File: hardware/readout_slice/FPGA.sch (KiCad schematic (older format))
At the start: 33 parts

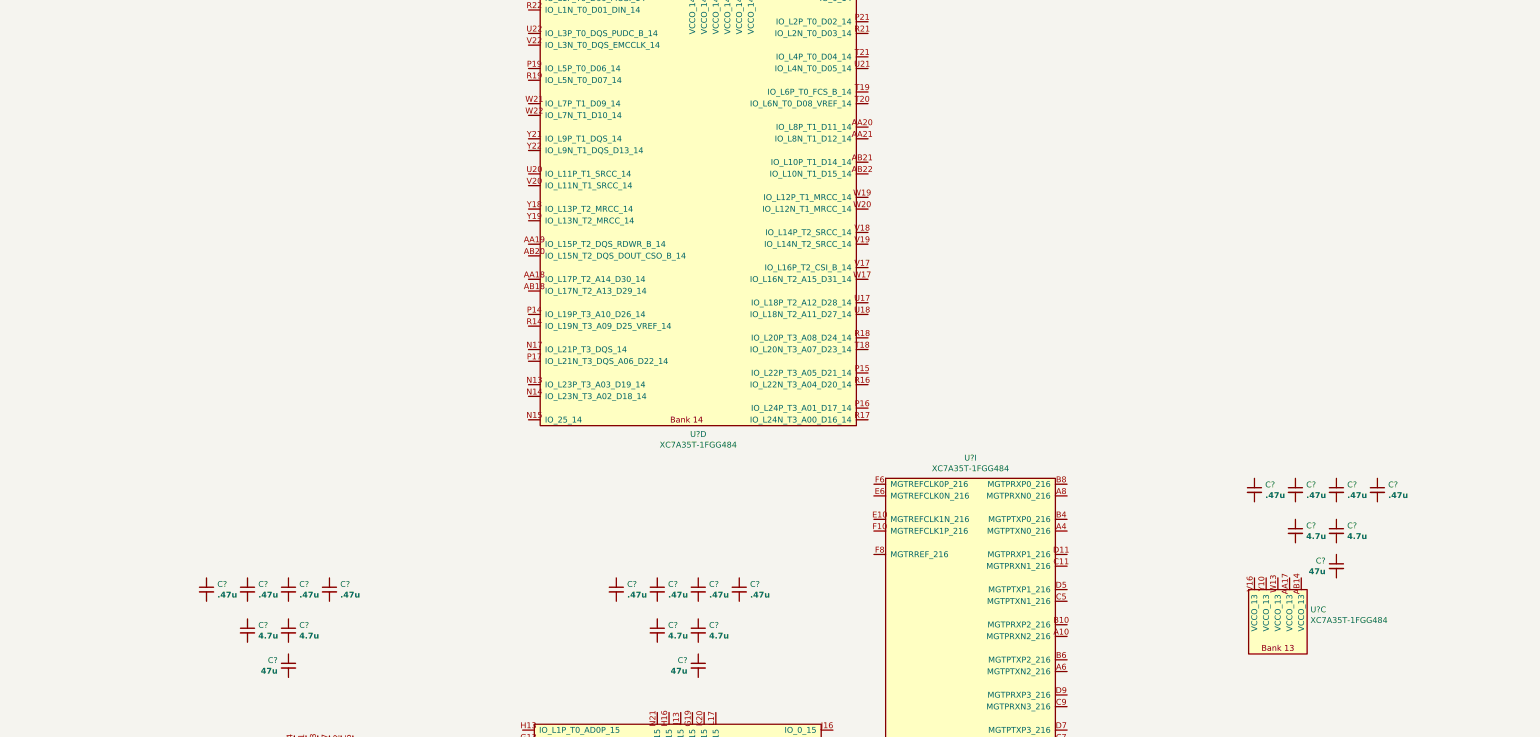
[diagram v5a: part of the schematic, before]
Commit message: readout_slice is more ordered now
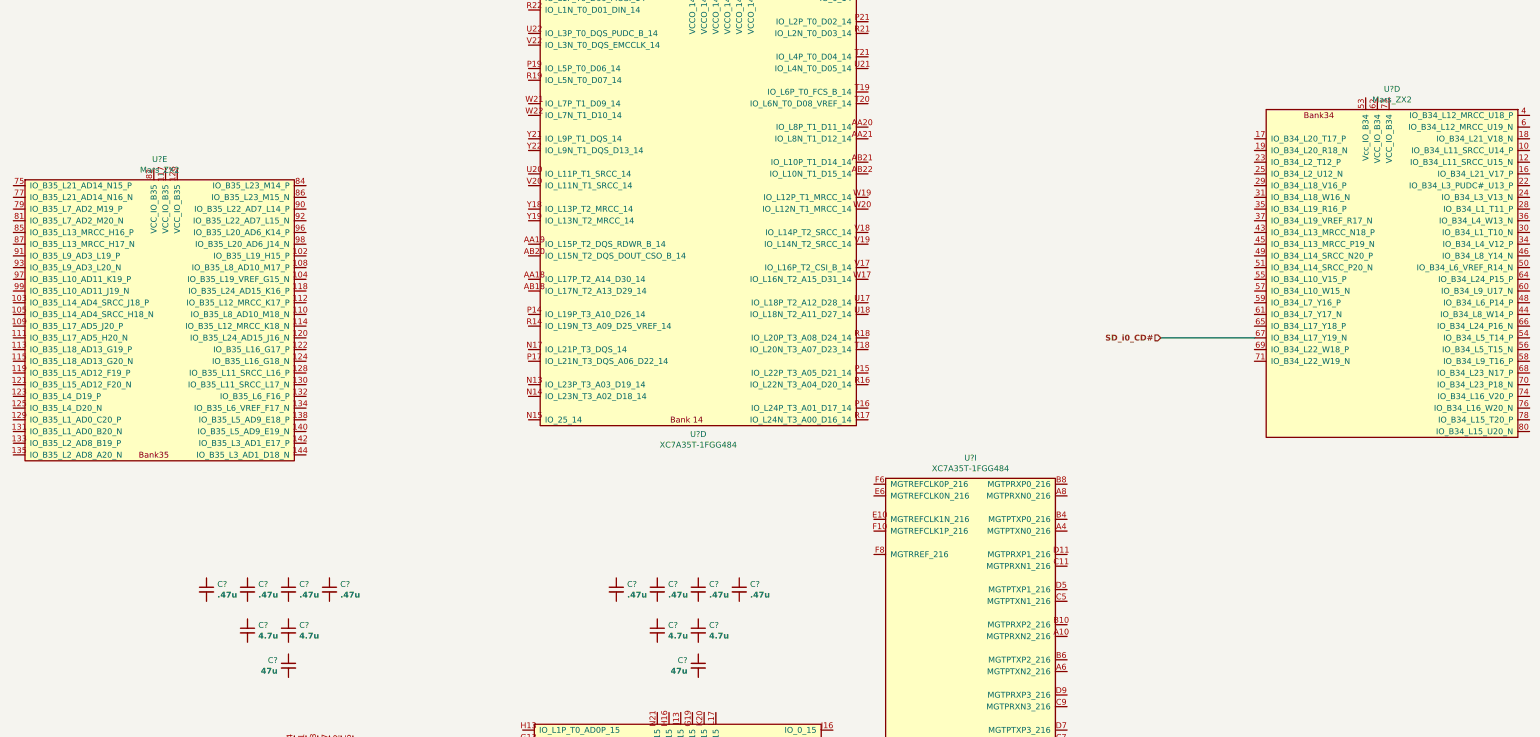
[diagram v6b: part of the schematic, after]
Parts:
- removed C?: 47u, symbol Device:C_Small
- removed C? (x2): 4.7u, symbol Device:C_Small
- removed C? (x4): .47u, symbol Device:C_Small
- removed U?: XC7A35T-1FGG484, symbol readout:XC7A35T-1FGG484
- added U? (x2): Mars_ZX2, Package_QFP:LQFP-160_24x24mm_P0.5mm, symbol readout:Mars_ZX2
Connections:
- new net SD_i0_CD#: U?.67 (IO_B34_L17_Y19_N)
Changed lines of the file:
@@
 $Descr A4 11693 8268
 encoding utf-8
-Sheet 3 6
+Sheet 2 10
 Title ""
 Date ""
@@
 $Comp
 L readout:XC7A35T-1FGG484 U?
-U 3 1 604BC08F
-P 10000 4800
-F 0 "U?" H 10278 4629 50  0000 L CNN
-F 1 "XC7A35T-1FGG484" H 10278 4538 50  0000 L CNN
-F 2 "" H 8900 4950 50  0001 C CNN
-F 3 "" H 8900 4950 50  0001 C CNN
-	3    10000 4800
-	1    0    0    -1
-$EndComp
-$Comp
-L readout:XC7A35T-1FGG484 U?
 U 4 1 604C5353
 P 5000 -300
@@
 	5500 -900 5500 -450
 Connection ~ 5500 -450
-$Comp
-L Device:C_Small C?
-U 1 1 6050AA4C
-P 10500 4600
-F 0 "C?" H 10408 4646 50  0000 R CNN
-F 1 "47u" H 10408 4555 50  0000 R CNB
-F 2 "" H 10500 4600 50  0001 C CNN
-F 3 "~" H 10500 4600 50  0001 C CNN
-	1    10500 4600
-	1    0    0    -1
-$EndComp
-$Comp
-L Device:C_Small C?
-U 1 1 6050AA52
-P 10500 4300
-F 0 "C?" H 10592 4346 50  0000 L CNN
-F 1 "4.7u" H 10592 4255 50  0000 L CNB
-F 2 "" H 10500 4300 50  0001 C CNN
-F 3 "~" H 10500 4300 50  0001 C CNN
-	1    10500 4300
-	1    0    0    -1
-$EndComp
-$Comp
-L Device:C_Small C?
-U 1 1 6050AA58
-P 10150 4300
-F 0 "C?" H 10242 4346 50  0000 L CNN
-F 1 "4.7u" H 10242 4255 50  0000 L CNB
-F 2 "" H 10150 4300 50  0001 C CNN
-F 3 "~" H 10150 4300 50  0001 C CNN
-	1    10150 4300
-	1    0    0    -1
-$EndComp
-$Comp
-L Device:C_Small C?
-U 1 1 6050AA5E
-P 9800 3950
-F 0 "C?" H 9892 3996 50  0000 L CNN
-F 1 ".47u" H 9892 3905 50  0000 L CNB
-F 2 "" H 9800 3950 50  0001 C CNN
-F 3 "~" H 9800 3950 50  0001 C CNN
-	1    9800 3950
-	1    0    0    -1
-$EndComp
-$Comp
-L Device:C_Small C?
-U 1 1 6050AA64
-P 10150 3950
-F 0 "C?" H 10242 3996 50  0000 L CNN
-F 1 ".47u" H 10242 3905 50  0000 L CNB
-F 2 "" H 10150 3950 50  0001 C CNN
-F 3 "~" H 10150 3950 50  0001 C CNN
-	1    10150 3950
-	1    0    0    -1
-$EndComp
-$Comp
-L Device:C_Small C?
-U 1 1 6050AA6A
-P 10500 3950
-F 0 "C?" H 10592 3996 50  0000 L CNN
-F 1 ".47u" H 10592 3905 50  0000 L CNB
-F 2 "" H 10500 3950 50  0001 C CNN
-F 3 "~" H 10500 3950 50  0001 C CNN
-	1    10500 3950
-	1    0    0    -1
-$EndComp
-$Comp
-L Device:C_Small C?
-U 1 1 6050AA70
-P 10850 3950
-F 0 "C?" H 10942 3996 50  0000 L CNN
-F 1 ".47u" H 10942 3905 50  0000 L CNB
-F 2 "" H 10850 3950 50  0001 C CNN
-F 3 "~" H 10850 3950 50  0001 C CNN
-	1    10850 3950
-	1    0    0    -1
-$EndComp
+Text HLabel 9000 2650 0    50   Input ~ 10
+SD_i0_CD#
+$Comp
+L readout:Mars_ZX2 U?
+U 4 1 6067D954
+P 11000 700
+AR Path="/6067D954" Ref="U?"  Part="4"
+AR Path="/605605C8/6067D954" Ref="U?"  Part="4"
+F 0 "U?" H 10975 875 50  0000 C CNN
+F 1 "Mars_ZX2" H 10975 784 50  0000 C CNN
+F 2 "Package_QFP:LQFP-160_24x24mm_P0.5mm" H 11050 1050 50  0001 C CNN
+F 3 "http://gauss.bu.edu/svn/emphatic-doco/Docs/CITIROC1A%20-%20Datasheet%20V2.5.pdf" H 11050 1050 50  0001 C CNN
+	4    11000 700
+	1    0    0    -1
+$EndComp
+Wire Wire Line
+	9800 2650 9000 2650
+$Comp
+L readout:Mars_ZX2 U?
+U 5 1 60BC92AD
+P 400 1300
+F 0 "U?" H 450 1475 50  0000 C CNN
+F 1 "Mars_ZX2" H 450 1384 50  0000 C CNN
+F 2 "Package_QFP:LQFP-160_24x24mm_P0.5mm" H 450 1650 50  0001 C CNN
+F 3 "http://gauss.bu.edu/svn/emphatic-doco/Docs/CITIROC1A%20-%20Datasheet%20V2.5.pdf" H 450 1650 50  0001 C CNN
+	5    400  1300
+	1    0    0    -1
+$EndComp
